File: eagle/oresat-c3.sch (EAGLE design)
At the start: 161 parts, among them J1 J-SAMTEC-TFM-110-X1-XXX-D-RA, J10 U.FL, J11 U.FL, J13 U.FL, J14 U.FL, J15 HARWIN-2X8X1.27, J19 HARWIN-2X8X1.27, J2 U.FL, J3 U.FL, J4 U.FL, J5 2-1734592-0, J6 J-SAMTEC-TFM-120-X1-XXX-D-RA, J8 U.FL, J9 U.FL, Q1 MOSFET-PCH-SOT23-6, U1 MAX892LEUA+T21-0036K-L, U11 U-ONSEMI-AX5043, U12 LP2985XX-N, U13 U-ONSEMI-AX5043, U14 LP2985XX-N, U2 TCAN330, U3 TCAN330, U4 TPS259621 - eFuse, U5 TPS62111RSA, U7 STM32F446RE, U8 UT01VS33DFLATDI_8, U9 SFEM016GB1EM1TO-A-HG-111-STD, X1 16MHZ-2.5x2mm, X3 TAITIEN-TY, X4 TAITIEN-TY

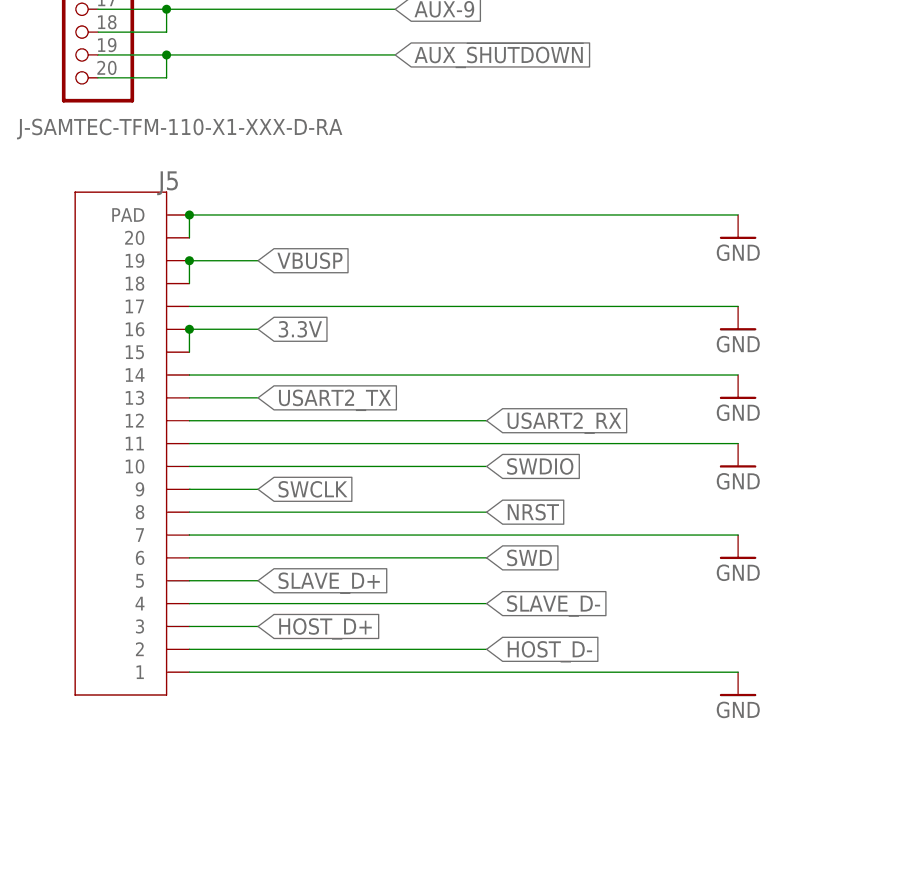
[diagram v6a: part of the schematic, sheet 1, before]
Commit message: Minor adjustments
Minor adjustments to edge connector and  labeling, shifted some of the Watchdog circuit
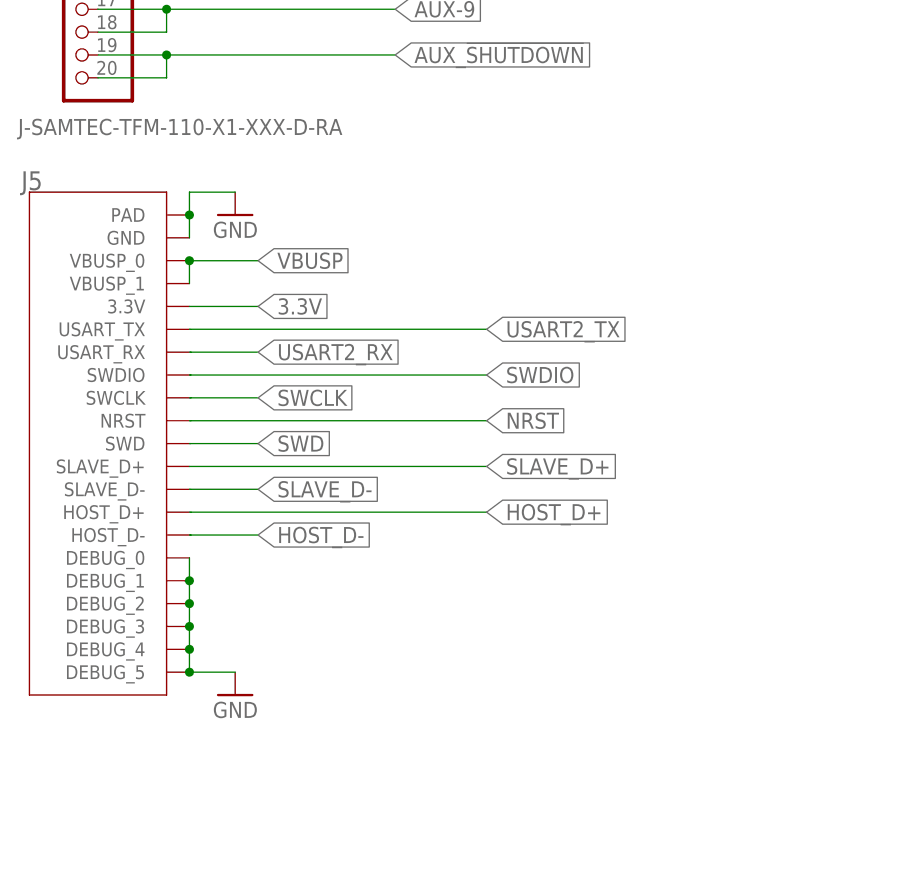
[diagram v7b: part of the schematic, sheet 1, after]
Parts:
- J5: device J-TEConnectivity-X-1734592-X:2-1734592-0 -> oresat-edge_connector:2-1734592-0
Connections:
- net 3.3V: now also J5.3.3V; no longer J5.15, J5.16
- net GND: now also J5.DEBUG_0, J5.DEBUG_1, J5.DEBUG_2, J5.DEBUG_3, J5.DEBUG_4, J5.DEBUG_5, J5.GND; no longer J5.1, J5.11, J5.14, J5.17, J5.20, J5.7
- net HOST_D+: now also J5.HOST_D+; no longer J5.3
- net HOST_D-: now also J5.HOST_D-; no longer J5.2
- net NRST: now also J5.NRST; no longer J5.8
- net SLAVE_D+: now also J5.SLAVE_D+; no longer J5.5
- net SLAVE_D-: now also J5.SLAVE_D-; no longer J5.4
- net SWCLK: now also J5.SWCLK; no longer J5.9
- net SWD: now also J5.SWD; no longer J5.6
- net SWDIO: now also J5.SWDIO; no longer J5.10
- net USART2_RX: now also J5.USART_RX; no longer J5.12
- net USART2_TX: now also J5.USART_TX; no longer J5.13
- net VBUSP: now also J5.VBUSP_0, J5.VBUSP_1; no longer J5.18, J5.19
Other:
- moved on the sheet: J5

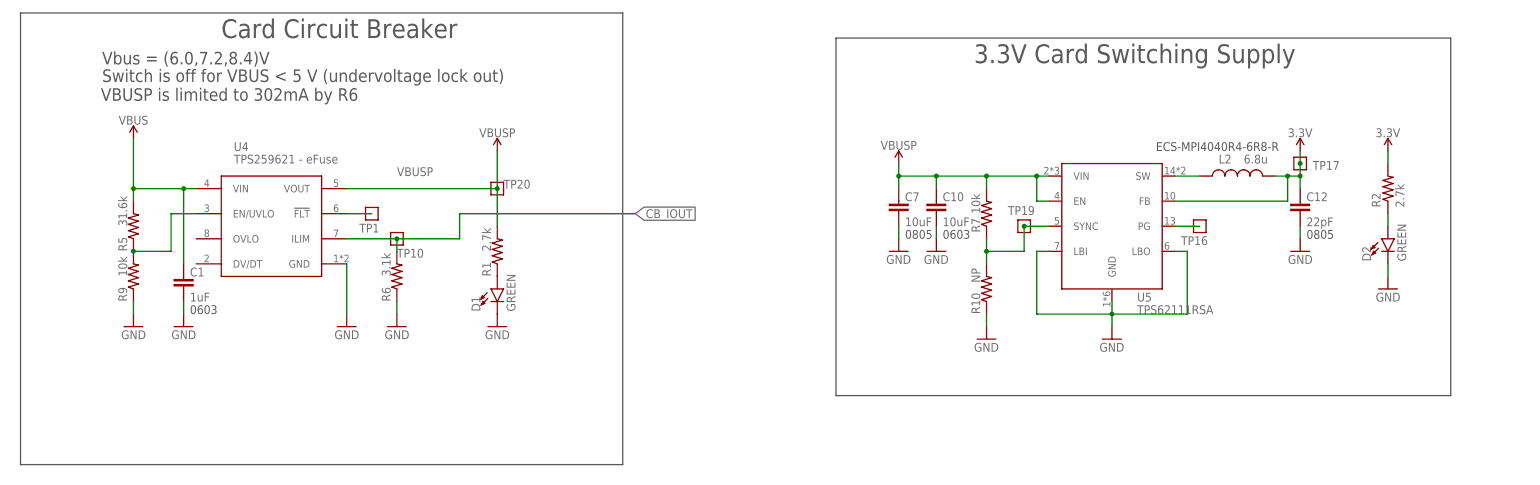
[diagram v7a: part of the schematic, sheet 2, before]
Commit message: Added 0 ohm resistor to section off VBUSP
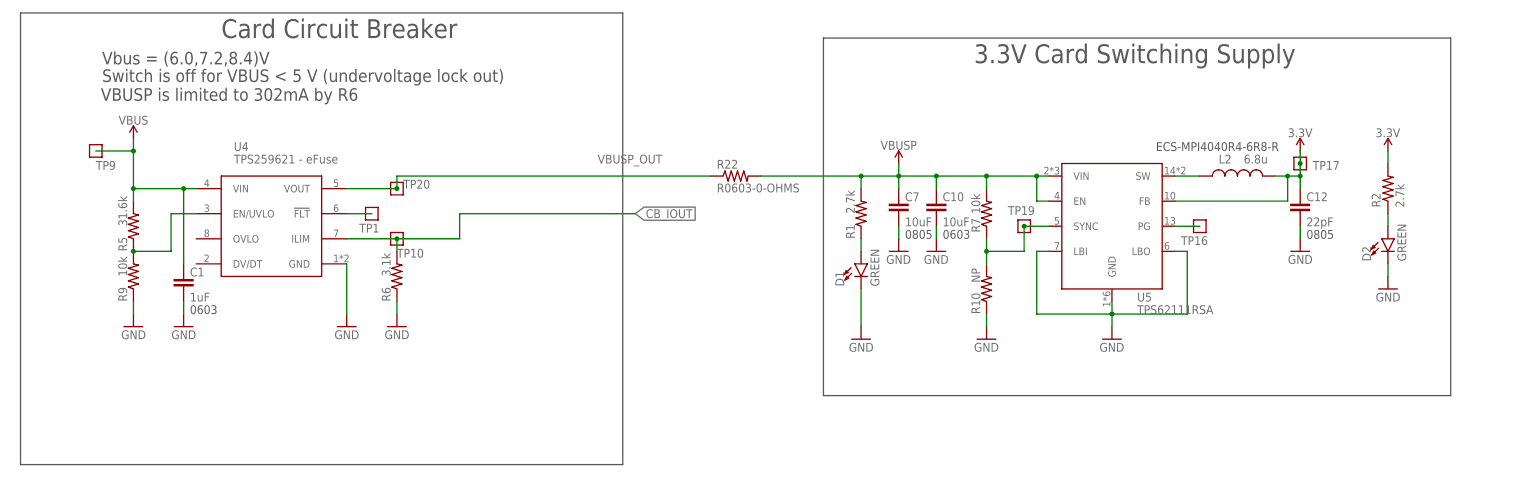
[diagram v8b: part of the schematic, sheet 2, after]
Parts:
- added R22: R0603-0-OHMS, C3_SamacSys_Parts:R0603-0-OHMS
- added TP9: VBUS, Tova:TEST-POINT
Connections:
- new net VBUSP_OUT: R22.1, TP20.1, U4.VOUT
- net VBUS: now also TP9.1
- net VBUSP: now also R22.2; no longer TP20.1, U4.VOUT
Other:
- moved on the sheet: D1, R1, TP20
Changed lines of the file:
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@@
 <part name="TP10" library="Tova" deviceset="TEST-POINT" device=""/>
 <part name="TP20" library="Tova" deviceset="TEST-POINT" device=""/>
-<part name="VBUSP1" library="oresat-supplies" deviceset="VBUSP" device=""/>
 <part name="VBUS1" library="oresat-supplies" deviceset="VBUS" device=""/>
 <part name="C6" library="C3_SamacSys_Parts" deviceset="CAP0603-0.1UF" device="" value="0.1uf">
@@
 <part name="R21" library="C3_SamacSys_Parts" deviceset="R0603-4.7K-OHMS" device="" value="4.7k"/>
 <part name="J5" library="oresat-edge_connector" deviceset="2-1734592-0" device=""/>
+<part name="TP9" library="Tova" deviceset="TEST-POINT" device="" value="VBUS"/>
+<part name="R22" library="C3_SamacSys_Parts" deviceset="R0603-0-OHMS" device=""/>
 </parts>
 <sheets>
@@
 <text x="275.59" y="223.52" size="1.778" layer="97">ECS-MPI4040R4-6R8-R</text>
 <text x="238.76" y="241.3" size="3.81" layer="97">3.3V Card Switching Supply</text>
-<wire x1="210.82" y1="246.38" x2="335.28" y2="246.38" width="0.1524" layer="97"/>
+<wire x1="208.28" y1="246.38" x2="335.28" y2="246.38" width="0.1524" layer="97"/>
 <wire x1="335.28" y1="246.38" x2="335.28" y2="173.99" width="0.1524" layer="97"/>
-<wire x1="335.28" y1="173.99" x2="210.82" y2="173.99" width="0.1524" layer="97"/>
-<wire x1="210.82" y1="173.99" x2="210.82" y2="246.38" width="0.1524" layer="97"/>
+<wire x1="335.28" y1="173.99" x2="208.28" y2="173.99" width="0.1524" layer="97"/>
+<wire x1="208.28" y1="173.99" x2="208.28" y2="246.38" width="0.1524" layer="97"/>
 <text x="416.56" y="6.35" size="3.81" layer="94">3.1</text>
 <text x="62.23" y="241.046" size="2.54" layer="97">Vbus = (6.0,7.2,8.4)V</text>
@@
 <attribute name="NAME" x="121.92" y="201.93" size="1.778" layer="95" font="vector"/>
 </instance>
-<instance part="TP20" gate="G$1" x="142.24" y="215.9" smashed="yes">
-<attribute name="NAME" x="143.51" y="215.9" size="1.778" layer="95" font="vector"/>
-</instance>
-<instance part="VBUSP1" gate="G$1" x="142.24" y="223.52" smashed="yes">
-<attribute name="VALUE" x="142.24" y="226.314" size="1.778" layer="96" align="bottom-center"/>
+<instance part="TP20" gate="G$1" x="121.92" y="215.9" smashed="yes">
+<attribute name="NAME" x="123.19" y="215.9" size="1.778" layer="95" font="vector"/>
 </instance>
 <instance part="VBUS1" gate="1" x="68.58" y="228.6" smashed="yes">
 <attribute name="VALUE" x="68.58" y="228.854" size="1.778" layer="96" align="bottom-center"/>
 </instance>
-<instance part="D1" gate="G$1" x="142.24" y="195.58" smashed="yes">
-<attribute name="NAME" x="138.811" y="191.008" size="1.778" layer="95" font="vector" rot="R90"/>
-<attribute name="VALUE" x="144.145" y="191.008" size="1.778" layer="96" font="vector" rot="R90" align="top-left"/>
-</instance>
-<instance part="GND7" gate="1" x="142.24" y="187.96" smashed="yes" rot="MR0">
-<attribute name="VALUE" x="144.78" y="185.42" size="1.778" layer="96" rot="MR0"/>
-</instance>
-<instance part="R1" gate="G$1" x="142.24" y="203.2" smashed="yes" rot="R90">
-<attribute name="DIS" x="142.24" y="203.2" size="1.778" layer="96" rot="R90" display="off"/>
-<attribute name="DPN" x="142.24" y="203.2" size="1.778" layer="96" rot="R90" display="off"/>
-<attribute name="MFR" x="142.24" y="203.2" size="1.778" layer="96" rot="R90" display="off"/>
-<attribute name="MPN" x="142.24" y="203.2" size="1.778" layer="96" rot="R90" display="off"/>
-<attribute name="NAME" x="140.97" y="198.12" size="1.778" layer="95" rot="R90"/>
-<attribute name="VALUE" x="140.97" y="203.2" size="1.778" layer="96" rot="R90"/>
+<instance part="D1" gate="G$1" x="215.9" y="200.66" smashed="yes">
+<attribute name="NAME" x="212.471" y="196.088" size="1.778" layer="95" font="vector" rot="R90"/>
+<attribute name="VALUE" x="217.805" y="196.088" size="1.778" layer="96" font="vector" rot="R90" align="top-left"/>
+</instance>
+<instance part="GND7" gate="1" x="215.9" y="185.42" smashed="yes" rot="MR0">
+<attribute name="VALUE" x="218.44" y="182.88" size="1.778" layer="96" rot="MR0"/>
+</instance>
+<instance part="R1" gate="G$1" x="215.9" y="210.82" smashed="yes" rot="R90">
+<attribute name="DIS" x="215.9" y="210.82" size="1.778" layer="96" rot="R90" display="off"/>
+<attribute name="DPN" x="215.9" y="210.82" size="1.778" layer="96" rot="R90" display="off"/>
+<attribute name="MFR" x="215.9" y="210.82" size="1.778" layer="96" rot="R90" display="off"/>
+<attribute name="MPN" x="215.9" y="210.82" size="1.778" layer="96" rot="R90" display="off"/>
+<attribute name="NAME" x="214.63" y="205.74" size="1.778" layer="95" rot="R90"/>
+<attribute name="VALUE" x="214.63" y="210.82" size="1.778" layer="96" rot="R90"/>
 </instance>
 <instance part="R5" gate="G$1" x="68.58" y="208.28" smashed="yes" rot="R90">
@@
 <attribute name="NAME" x="80.01" y="198.12" size="1.778" layer="95"/>
 <attribute name="VALUE" x="80.01" y="193.04" size="1.778" layer="96"/>
+</instance>
+<instance part="TP9" gate="G$1" x="60.96" y="223.52" smashed="yes">
+<attribute name="NAME" x="60.96" y="219.71" size="1.778" layer="95" font="vector"/>
+</instance>
+<instance part="R22" gate="G$1" x="190.5" y="218.44" smashed="yes">
+<attribute name="NAME" x="186.69" y="219.9386" size="1.778" layer="95"/>
+<attribute name="VALUE" x="186.69" y="215.138" size="1.778" layer="96"/>
 </instance>
 </instances>
@@
 <pinref part="D1" gate="G$1" pin="C"/>
 <pinref part="GND7" gate="1" pin="GND"/>
+<wire x1="215.9" y1="195.58" x2="215.9" y2="187.96" width="0.1524" layer="91"/>
 </segment>
 <segment>
@@
 <net name="VBUSP" class="0">
 <segment>
+<pinref part="R22" gate="G$1" pin="2"/>
+<wire x1="195.58" y1="218.44" x2="215.9" y2="218.44" width="0.1524" layer="91"/>
 <pinref part="VBUSP2" gate="G$1" pin="VBUSP"/>
 <pinref part="U5" gate="G$1" pin="VIN"/>
+<wire x1="215.9" y1="218.44" x2="223.52" y2="218.44" width="0.1524" layer="91"/>
 <wire x1="254" y1="218.44" x2="251.46" y2="218.44" width="0.1524" layer="91"/>
 <pinref part="U5" gate="G$1" pin="EN"/>
@@
 <pinref part="C7" gate="G$1" pin="1"/>
 <wire x1="223.52" y1="215.9" x2="223.52" y2="218.44" width="0.1524" layer="91"/>
-</segment>
-<segment>
-<pinref part="TP20" gate="G$1" pin="1"/>
-<junction x="142.24" y="215.9"/>
-<wire x1="111.76" y1="215.9" x2="142.24" y2="215.9" width="0.1524" layer="91"/>
-<pinref part="VBUSP1" gate="G$1" pin="VBUSP"/>
-<wire x1="142.24" y1="215.9" x2="142.24" y2="223.52" width="0.1524" layer="91"/>
-<label x="121.92" y="218.44" size="1.778" layer="95"/>
 <pinref part="R1" gate="G$1" pin="2"/>
-<wire x1="142.24" y1="215.9" x2="142.24" y2="208.28" width="0.1524" layer="91"/>
-<pinref part="U4" gate="G$1" pin="VOUT"/>
+<wire x1="215.9" y1="215.9" x2="215.9" y2="218.44" width="0.1524" layer="91"/>
+<junction x="215.9" y="218.44"/>
 </segment>
 </net>
@@
 <pinref part="D1" gate="G$1" pin="A"/>
 <pinref part="R1" gate="G$1" pin="1"/>
+<wire x1="215.9" y1="205.74" x2="215.9" y2="203.2" width="0.1524" layer="91"/>
 </segment>
 </net>
@@
 <pinref part="VBUS1" gate="1" pin="VBUS"/>
 <wire x1="81.28" y1="215.9" x2="78.74" y2="215.9" width="0.1524" layer="91"/>
-<wire x1="68.58" y1="226.06" x2="68.58" y2="215.9" width="0.1524" layer="91"/>
+<wire x1="68.58" y1="226.06" x2="68.58" y2="223.52" width="0.1524" layer="91"/>
 <junction x="68.58" y="215.9"/>
 <pinref part="U4" gate="G$1" pin="VIN"/>
 <pinref part="C1" gate="G$1" pin="1"/>
+<pinref part="TP9" gate="G$1" pin="1"/>
+<wire x1="68.58" y1="223.52" x2="68.58" y2="215.9" width="0.1524" layer="91"/>
+<wire x1="60.96" y1="223.52" x2="68.58" y2="223.52" width="0.1524" layer="91"/>
+<junction x="68.58" y="223.52"/>
 </segment>
 </net>
@@
 </segment>
 </net>
+<net name="VBUSP_OUT" class="0">
+<segment>
+<pinref part="TP20" gate="G$1" pin="1"/>
+<junction x="121.92" y="215.9"/>
+<wire x1="111.76" y1="215.9" x2="121.92" y2="215.9" width="0.1524" layer="91"/>
+<label x="162.56" y="220.98" size="1.778" layer="95"/>
+<pinref part="U4" gate="G$1" pin="VOUT"/>
+<wire x1="121.92" y1="215.9" x2="121.92" y2="218.44" width="0.1524" layer="91"/>
+<pinref part="R22" gate="G$1" pin="1"/>
+<wire x1="121.92" y1="218.44" x2="185.42" y2="218.44" width="0.1524" layer="91"/>
+</segment>
+</net>
